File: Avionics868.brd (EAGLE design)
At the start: 86.4 x 22.9 mm, 69 parts, among them SW1 B3U-1000P-2P-SMD, U1 ATSAMD21G18_QFN, U2 SPX3819M5-L-3-0, U3 MCP73831T-2ACI/OT, U4 MPU-9250, U5 SIM868, U6 BMP280, X1 JSTPH, X2 32.768, X3 ZX62-B-5PA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

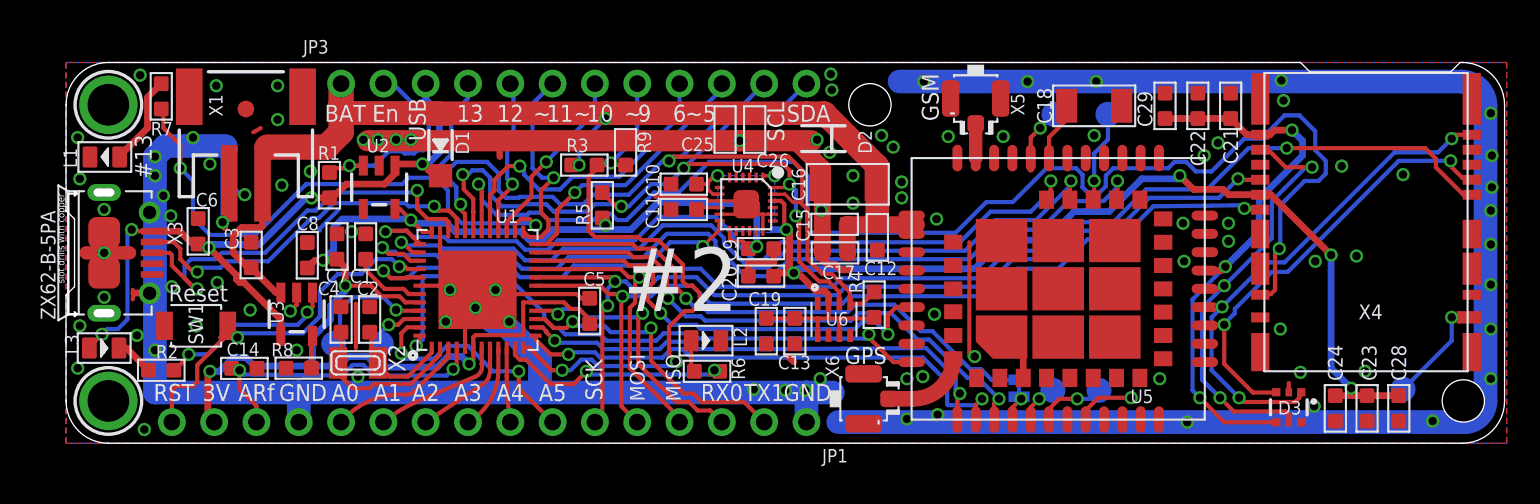
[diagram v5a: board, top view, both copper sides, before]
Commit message: Shrunk the board some mils horizontally
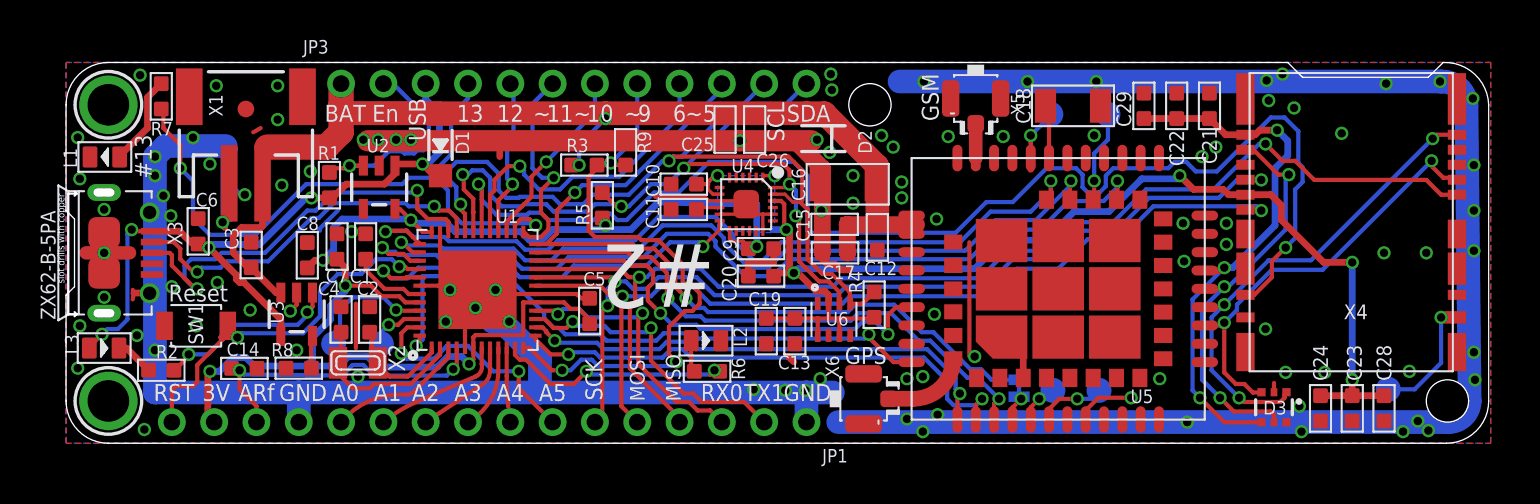
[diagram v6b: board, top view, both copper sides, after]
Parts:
- moved C18 1.27 mm to (60.5, 20.3)
- moved C21 1.27 mm to (68.6, 20.3)
- moved C22 1.27 mm to (66.7, 20.3)
- moved C29 1.27 mm to (64.7, 20.3)
- moved C23 0.89 mm to (77.2, 2.10)
- moved C28 0.89 mm to (79.1, 2.10)
- moved D3 0.89 mm to (72.5, 2.16)
- moved C24 0.89 mm to (75.3, 2.10)
- moved TP3 0.89 mm to (79.4, 3.24)
- moved X4 0.89 mm to (77.2, 13.3)
- moved TP5 0.19 mm to (59.1, 19.7)
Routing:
- net SIM_RST: track 27.0 -> 24.7 mm
- net GND: track 262.6 -> 260.5 mm, vias 98 -> 104
- net D7/SD_CS: track 78.4 -> 76.4 mm
- net SIM_CLK: track 30.9 -> 29.3 mm
- net SIM_DATA: track 27.2 -> 25.8 mm
- net SCK: track 56.4 -> 57.4 mm
- net MISO: track 72.2 -> 71.2 mm
- net MOSI: track 55.1 -> 56.0 mm
- net SD_DET: track 6.56 -> 7.34 mm
- net +3V: track 157.6 -> 158.3 mm
- net SIM_VDD: track 33.9 -> 33.2 mm
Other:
- board size 86.4 x 22.9 mm -> 85.4 x 22.9 mm

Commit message: Made it even a tiny bit shorter
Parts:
- moved X4 0.18 mm to (77.0, 13.1)
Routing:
- net +3V: track 158.3 -> 170.0 mm
- net SIM_CLK: track 29.3 -> 31.8 mm
- net SIM_DATA: track 25.8 -> 27.9 mm
- net SD_DET: track 7.34 -> 6.68 mm
- net GND: track 260.5 -> 259.9 mm
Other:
- board size 85.4 x 22.9 mm -> 85.1 x 22.9 mm

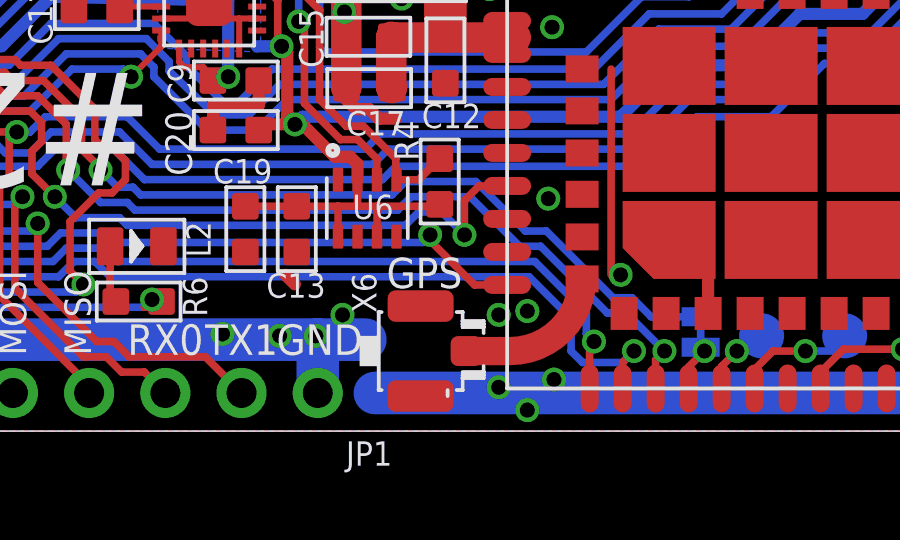
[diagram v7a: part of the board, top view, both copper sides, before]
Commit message: Tweaked GPS antenna trace
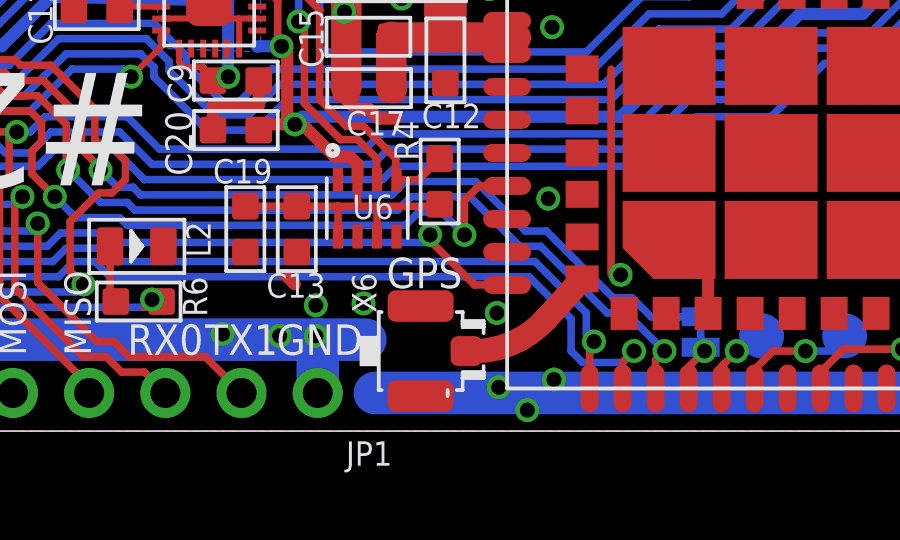
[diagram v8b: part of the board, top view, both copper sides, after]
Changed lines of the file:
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@@
 <wire x1="44.45" y1="3.048" x2="46.0375" y2="3.048" width="1.4224" layer="16"/>
 <via x="54.5465" y="5.207" extent="1-16" drill="0.5"/>
-<via x="50.4825" y="3.8735" extent="1-16" drill="0.5"/>
 <via x="0.6985" y="4.5085" extent="1-16" drill="0.5"/>
 <via x="4.699" y="0.8255" extent="1-16" drill="0.5"/>
@@
 <via x="50.4825" y="1.4605" extent="1-16" drill="0.5"/>
 <via x="52.324" y="1.7145" extent="1-16" drill="0.5"/>
-<via x="45.2755" y="3.8735" extent="1-16" drill="0.5"/>
+<via x="44.3865" y="4.191" extent="1-16" drill="0.5"/>
 <via x="45.339" y="13.97" extent="1-16" drill="0.5"/>
 <via x="47.244" y="14.4145" extent="1-16" drill="0.5"/>
@@
 <via x="44.3865" y="3.175" extent="1-16" drill="0.5"/>
 <via x="40.4495" y="18.161" extent="1-16" drill="0.5"/>
-<via x="51.435" y="4.0005" extent="1-16" drill="0.5"/>
 <wire x1="13.843" y1="9.0471" x2="13.843" y2="8.3185" width="0.254" layer="1"/>
 <wire x1="13.843" y1="8.3185" x2="13.462" y2="7.9375" width="0.254" layer="1"/>
@@
 <via x="76.581" y="18.6055" extent="1-16" drill="0.5"/>
 <via x="82.2325" y="21.2725" extent="1-16" drill="0.5"/>
-<wire x1="42.4815" y1="11.684" x2="42.4815" y2="11.6205" width="0" layer="19" extent="1-1"/>
 <via x="79.121" y="11.2395" extent="1-16" drill="0.5"/>
 <via x="76.327" y="11.2395" extent="1-16" drill="0.5"/>
 <via x="79.121" y="14.732" extent="1-16" drill="0.5"/>
+<via x="45.974" y="4.2545" extent="1-16" drill="0.5"/>
+<via x="50.419" y="3.937" extent="1-16" drill="0.5"/>
+<wire x1="50.4825" y1="1.4605" x2="50.419" y2="3.937" width="0" layer="19" extent="1-1"/>
+<wire x1="42.4815" y1="11.684" x2="42.4815" y2="11.6205" width="0" layer="19" extent="1-1"/>
 </signal>
 <signal name="MOSI">
@@
 <contactref element="X6" pad="D"/>
 <contactref element="U5" pad="68_"/>
-<wire x1="49.403" y1="2.667" x2="50.859" y2="2.667" width="0.94" layer="1"/>
-<wire x1="50.859" y1="2.667" x2="53.263" y2="5.071" width="0.94" layer="1" curve="90"/>
+<wire x1="52.07" y1="3.7465" x2="49.403" y2="2.667" width="0.8128" layer="1" curve="-51.907764"/>
+<wire x1="52.07" y1="3.7465" x2="53.263" y2="5.071" width="0.8128" layer="1"/>
 </signal>
 <signal name="GSM_ANT">
